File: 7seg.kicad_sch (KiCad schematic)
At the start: 6 parts, among them U2 74LS49, U3 74LS49, U4 D148K, U5 D148K

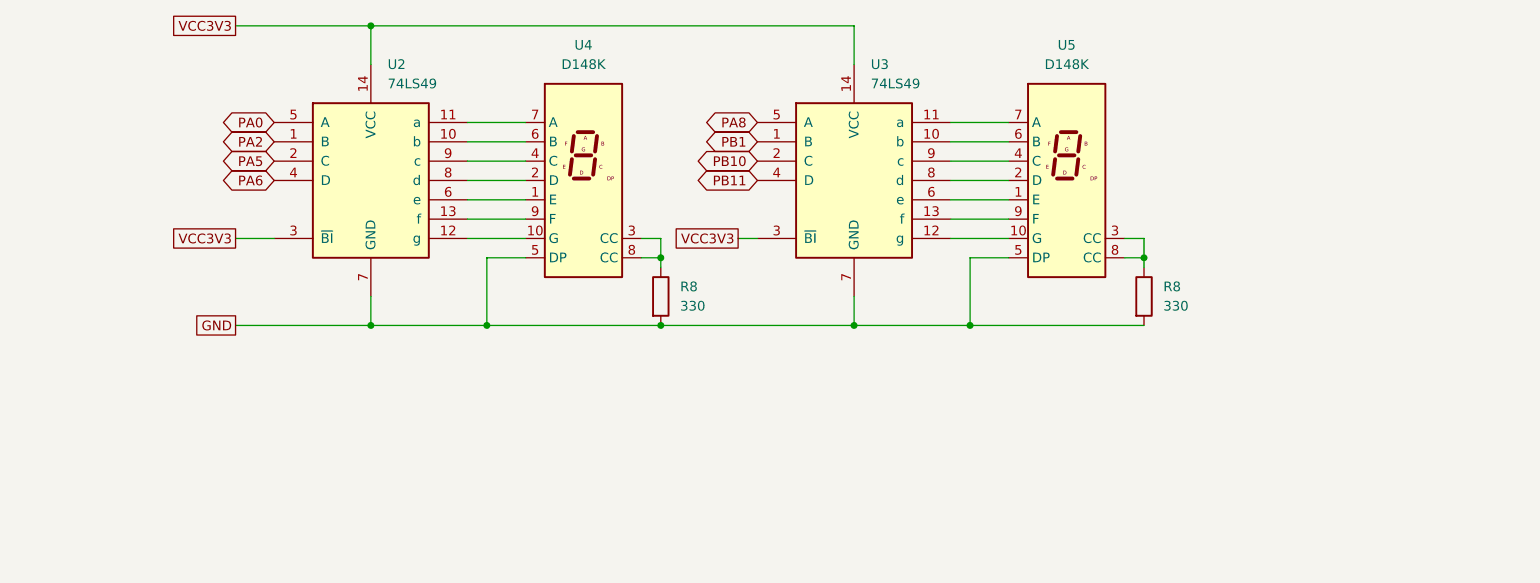
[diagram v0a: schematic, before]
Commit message: Changed segment display to TDSR1360
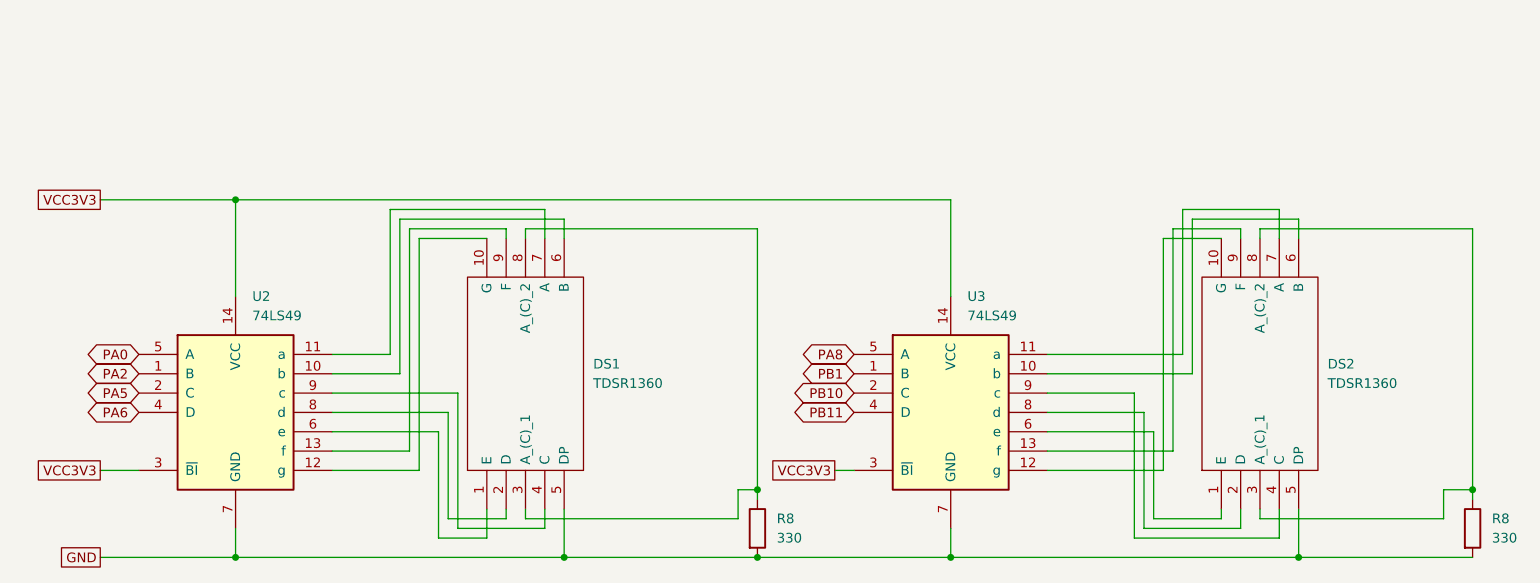
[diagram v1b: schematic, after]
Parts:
- removed U4, U5: D148K, Display_7Segment:D1X8K, symbol Display_Character:D148K
- added DS1, DS2: TDSR1360, DIPS1524W55P254L1225H710Q10N, symbol SamacSys_Parts:TDSR1360
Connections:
- net GND: now also DS1.5 (DP), DS2.5 (DP)
- net at R8.1: now also DS2.3 (A_(C)_1), DS2.8 (A_(C)_2)
- net at R8.1: now also DS1.3 (A_(C)_1), DS1.8 (A_(C)_2)
- net at U2.10 (b): now also DS1.6 (B)
- net at U2.11 (a): now also DS1.7 (A)
- net at U2.12 (g): now also DS1.10 (G)
- net at U2.13 (f): now also DS1.9 (F)
- net at U2.6 (e): now also DS1.1 (E)
- net at U2.8 (d): now also DS1.2 (D)
- net at U2.9 (c): now also DS1.4 (C)
- net at U3.6 (e): now also DS2.1 (E)
- net at U3.12 (g): now also DS2.10 (G)
- net at U3.8 (d): now also DS2.2 (D)
- net at U3.9 (c): now also DS2.4 (C)
- net at U3.10 (b): now also DS2.6 (B)
- net at U3.11 (a): now also DS2.7 (A)
- net at U3.13 (f): now also DS2.9 (F)
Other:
- moved on the sheet: R8, U2, U3
